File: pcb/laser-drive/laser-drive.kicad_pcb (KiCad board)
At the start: 2 copper layers, 28.6 x 32.4 mm, 29 parts, among them J1 CONN_01X03, P1 LaserOut, Q1 BCP5616Q, Q2 MTM232270, U2 MIC920

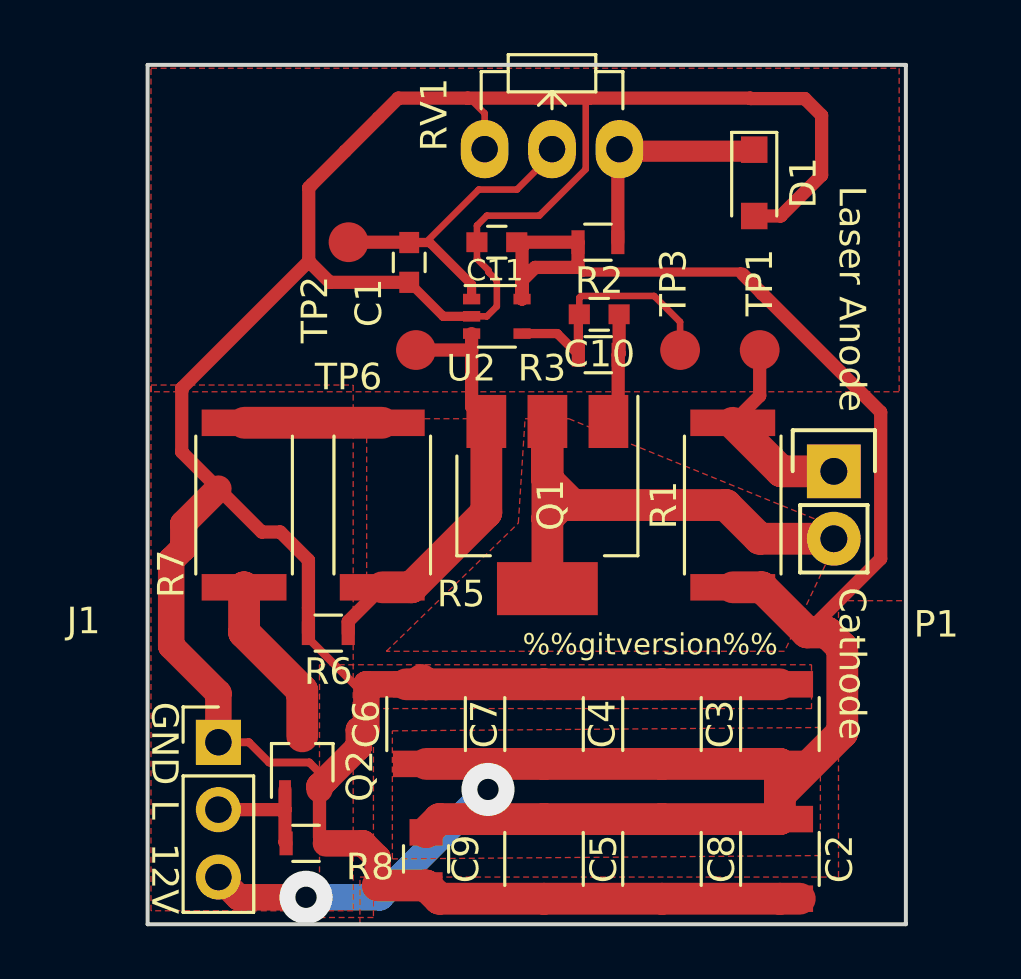
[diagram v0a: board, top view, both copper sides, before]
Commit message: Laser driver: Update to current KiCAD
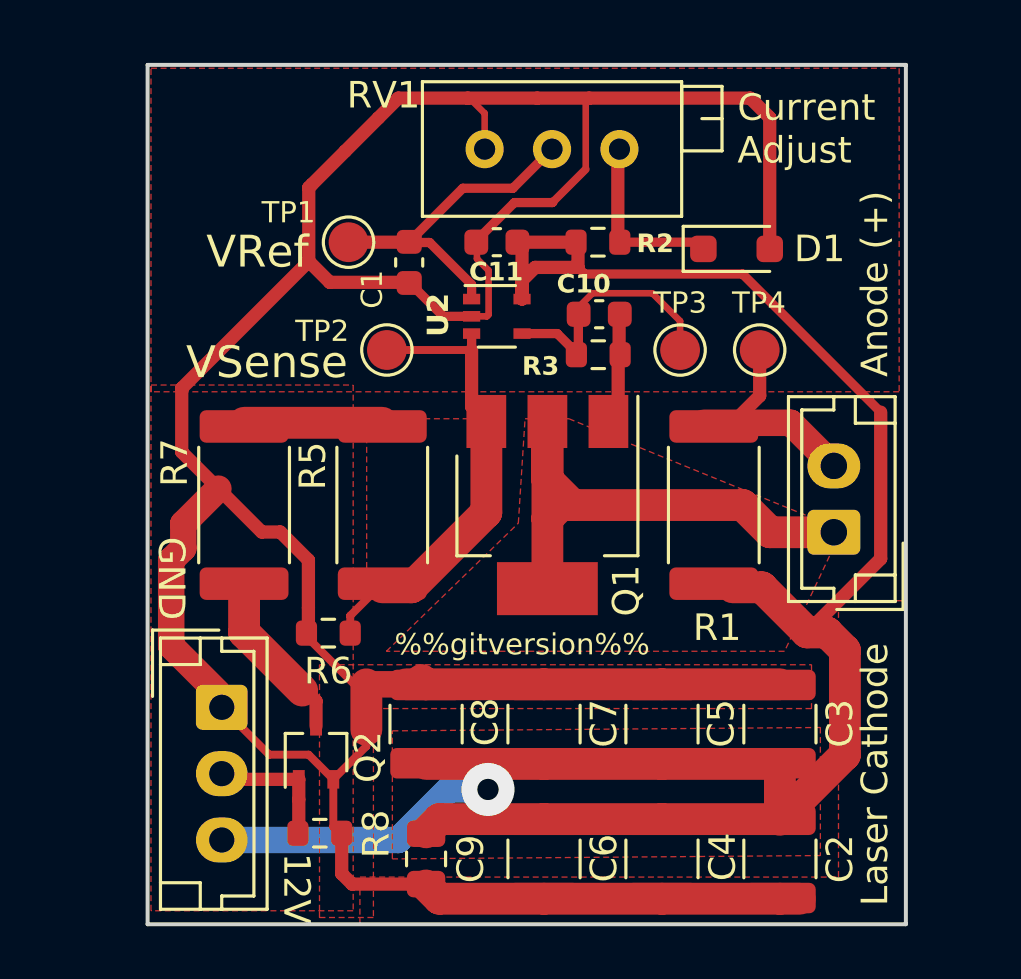
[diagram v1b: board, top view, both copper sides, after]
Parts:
- C1, C10, C11: footprint Capacitors_SMD:C_0603 -> Capacitor_SMD:C_0603_1608Metric
- C2, C3, C4, C5, C6, C7, C8: footprint Capacitors_SMD:C_1210 -> Capacitor_SMD:C_1210_3225Metric
- C9: footprint Capacitors_SMD:C_0805 -> Capacitor_SMD:C_0805_2012Metric
- D1: footprint Diodes_SMD:D_SOD-323_HandSoldering -> Diode_SMD:D_SOD-323_HandSoldering
- J1: footprint Pin_Headers:Pin_Header_Straight_1x03_Pitch2.54mm -> Connector_JST:JST_EH_B3B-EH-A_1x03_P2.50mm_Vertical
- P1: footprint Pin_Headers:Pin_Header_Straight_1x02 -> Connector_JST:JST_EH_B2B-EH-A_1x02_P2.50mm_Vertical
- Q1: footprint TO_SOT_Packages_SMD:SOT-223 -> Package_TO_SOT_SMD:SOT-223-3_TabPin2
- Q2: footprint TO_SOT_Packages_SMD:SOT-323_SC-70 -> Package_TO_SOT_SMD:SOT-323_SC-70
- R1, R5, R7: footprint Resistors_SMD:R_2512 -> Resistor_SMD:R_2512_6332Metric
- R2, R3, R6, R8: footprint Resistors_SMD:R_0603 -> Resistor_SMD:R_0603_1608Metric
- RV1: footprint Potentiometers:Potentiometer_WirePads_Small -> Potentiometer_THT:Potentiometer_Bourns_3296X_Horizontal
- TP1: renamed from TP2; footprint Measurement_Points:Measurement_Point_Round-SMD-Pad_Small -> TestPoint:TestPoint_Pad_D1.5mm
- TP2: renamed from TP6; footprint Measurement_Points:Measurement_Point_Round-SMD-Pad_Small -> TestPoint:TestPoint_Pad_D1.5mm
- TP3: footprint Measurement_Points:Measurement_Point_Round-SMD-Pad_Small -> TestPoint:TestPoint_Pad_D1.5mm
- TP4: renamed from TP1; footprint Measurement_Points:Measurement_Point_Round-SMD-Pad_Small -> TestPoint:TestPoint_Pad_D1.5mm
- U2: footprint TO_SOT_Packages_SMD:SOT-353_SC-70-5 -> Package_TO_SOT_SMD:SOT-353_SC-70-5
- moved C8 10.2 mm to (93.7, 69.9), turned to 90 degrees
- moved C5 6.75 mm to (102.6, 69.9), turned to 90 degrees
- moved C6 6.75 mm to (98.1, 75.0), turned to -90 degrees
- moved C4 5.08 mm to (102.6, 75.0), turned to -90 degrees
- moved D1 2.58 mm to (105.4, 52.0), turned to 0 degrees
- moved P1 2.30 mm to (109.0, 62.7), turned to 90 degrees
- moved J1 1.32 mm to (86.0, 69.3), turned to -90 degrees
- moved TP2 1.10 mm to (92.2, 55.8)
- moved R1 0.71 mm to (104.5, 61.7)
- moved R8 0.64 mm to (89.7, 74.0)
- moved Q2 0.64 mm to (89.5, 71.0)
- turned RV1 to 180 degrees
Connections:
- net Net-(C10-Pad2) renamed /ControlOut
- net Net-(D1-Pad1) renamed /Hot
- P1 pad 1: /CurrentTP -> /Laser-Cathode
- P1 pad 2: /LaserOut -> /Laser-Anode
- Q1 pad 2: /LaserOut -> /Laser-Cathode
- R1 pad 2: /CurrentTP -> /Laser-Anode
- TP4 pad 1: /CurrentTP -> /Laser-Anode
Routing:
- net /LaserOut: track 21.4 -> 0.00 mm
- net /Laser-Cathode: track 0.00 -> 21.3 mm
- net /Laser-Anode: track 0.00 -> 8.74 mm
- net /CurrentTP: track 7.73 -> 0.00 mm
- net GND: track 130.9 -> 125.9 mm
- net /Hot: track 9.19 -> 7.00 mm
- net /VRef: track 12.8 -> 13.5 mm
- net /VSense: track 17.0 -> 17.6 mm
- net +12V: track 85.8 -> 85.3 mm, vias 2 -> 1
- added copper zone on F.Cu, net /Laser-Cathode
- removed copper zone on F.Cu, net /LaserOut
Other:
- net class Default removed
- net class Power removed
- rule pad_to_mask_clearance: 0.2 -> 0.1
- board text added: "Anode (+)"
- board text added: "Current Adjust"
- board text added: "Laser Cathode"
- board text added: "VRef"
- board text added: "VSense"
- board text removed: "Cathode"
- board text removed: "L"
- board text removed: "Laser Anode"

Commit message: Update fab script to work with current KiCAD
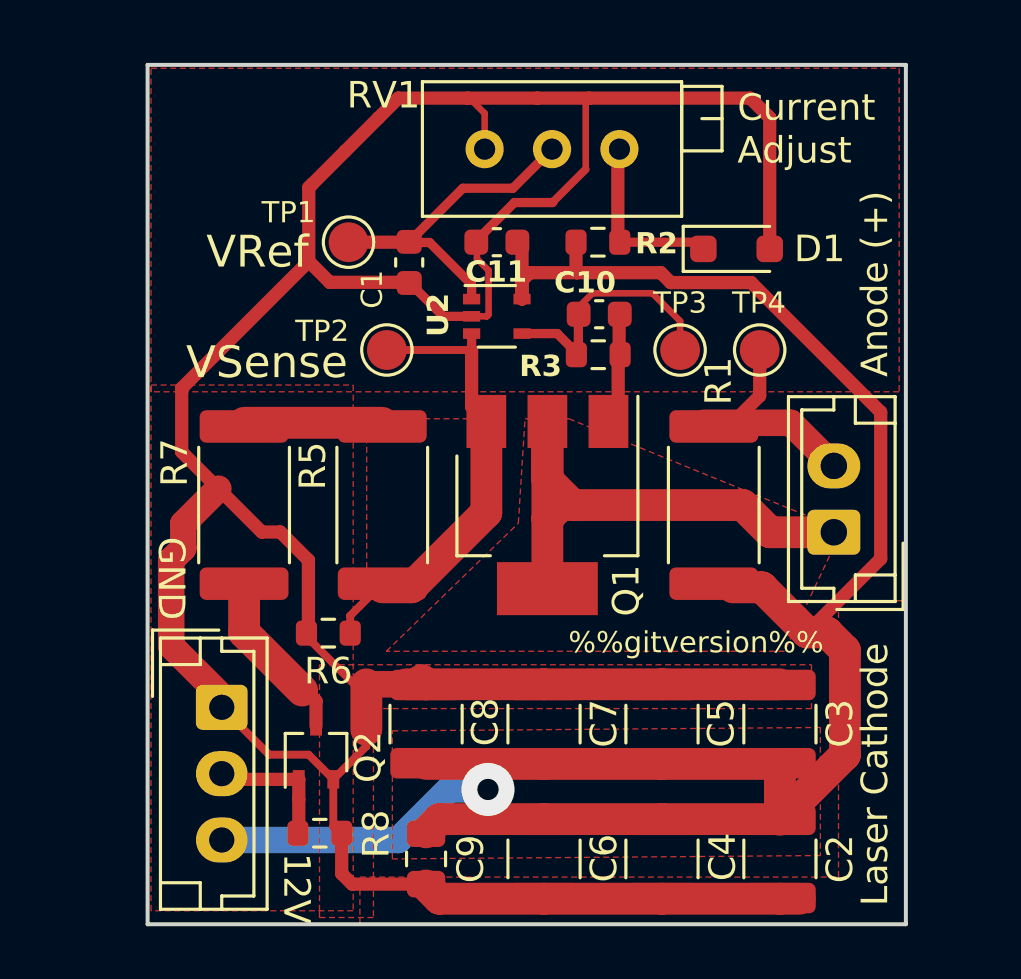
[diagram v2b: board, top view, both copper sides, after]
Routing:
- net +12V: track 85.3 -> 83.1 mm
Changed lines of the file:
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@@
     (attr smd)
     (fp_text reference "C11" (at -0.028287 1.115849 180) (layer "F.SilkS")
-        (effects (font (size 0.7 0.7) (thickness 0.12) bold))
+        (effects (font (size 0.8 0.8) (thickness 0.12) bold))
     )
     (fp_text value "100n" (at 0 1.43) (layer "F.Fab")
@@
     (property "Sheetname" "")
     (attr smd)
-    (fp_text reference "R1" (at -4.621049 0.127 180) (layer "F.SilkS")
+    (fp_text reference "R1" (at 4.675351 0.1778 90) (layer "F.SilkS")
         (effects (font (size 1 1) (thickness 0.15)))
     )
@@
     (attr smd)
     (fp_text reference "R3" (at 2.173887 -0.4318 180) (layer "F.SilkS")
-        (effects (font (size 0.7 0.7) (thickness 0.12) bold))
+        (effects (font (size 0.8 0.8) (thickness 0.12) bold))
     )
     (fp_text value "470" (at 0 1.43 180) (layer "F.Fab")
@@
     (property "Sheetname" "")
     (attr smd)
-    (fp_text reference "R2" (at 2.156113 0.049049) (layer "F.SilkS")
-        (effects (font (size 0.7 0.7) (thickness 0.12) bold))
+    (fp_text reference "R2" (at 2.206913 0.049049) (layer "F.SilkS")
+        (effects (font (size 0.8 0.8) (thickness 0.12) bold))
     )
     (fp_text value "2k2" (at 0 1.43) (layer "F.Fab")
@@
     (property "Sheetname" "")
     (attr smd)
-    (fp_text reference "C10" (at 0.5842 1.143 180) (layer "F.SilkS")
-        (effects (font (size 0.7 0.7) (thickness 0.12) bold))
+    (fp_text reference "C10" (at 0.5334 1.1938 180) (layer "F.SilkS")
+        (effects (font (size 0.8 0.8) (thickness 0.12) bold))
     )
     (fp_text value "100p" (at 0 1.43 180) (layer "F.Fab")
@@
     (effects (font (size 1 1) (thickness 0.2)) (justify left))
   )
-  (gr_text "%%gitversion%%" (at 102.108 66.929) (layer "F.SilkS")
+  (gr_text "%%gitversion%%" (at 108.6612 66.8528) (layer "F.SilkS")
     (effects (font (size 0.8 0.8) (thickness 0.15)) (justify right))
   )
@@
   (segment (start 93.515087 68.264951) (end 93.678087 68.427951) (width 1.2) (layer "F.Cu") (net 1))
   (segment (start 96.035088 52.831952) (end 96.035088 54.49595) (width 0.25) (layer "F.Cu") (net 1))
+  (segment (start 102.899216 53.2892) (end 102.526968 52.916952) (width 0.5) (layer "F.Cu") (net 2))
+  (segment (start 97.295087 53.210951) (end 97.295087 53.910951) (width 0.5) (layer "F.Cu") (net 2))
   (segment (start 109.463087 71.082951) (end 107.013087 73.532951) (width 1.2) (layer "F.Cu") (net 2))
-  (segment (start 97.295087 53.210951) (end 97.789087 52.716951) (width 0.5) (layer "F.Cu") (net 2))
-  (segment (start 108.035087 66.472951) (end 110.811088 63.69695) (width 0.5) (layer "F.Cu") (net 2))
-  (segment (start 99.405087 51.766951) (end 97.095087 51.766951) (width 0.5) (layer "F.Cu") (net 2))
   (segment (start 107.013087 72.594951) (end 107.013087 71.427951) (width 1.2) (layer "F.Cu") (net 2))
+  (segment (start 110.811088 58.17095) (end 105.929338 53.2892) (width 0.5) (layer "F.Cu") (net 2))
+  (segment (start 97.589086 52.916952) (end 97.295087 53.210951) (width 0.5) (layer "F.Cu") (net 2))
   (segment (start 96.012 73.45066) (end 95.954709 73.507951) (width 1) (layer "F.Cu") (net 2))
   (segment (start 108.035087 66.472951) (end 106.335087 64.772951) (width 1.2) (layer "F.Cu") (net 2))
   (segment (start 98.123087 71.427951) (end 93.678087 71.427951) (width 1.2) (layer "F.Cu") (net 2))
+  (segment (start 99.330087 51.766951) (end 99.330087 52.882239) (width 0.5) (layer "F.Cu") (net 2))
   (segment (start 94.178087 73.507951) (end 93.678087 74.007951) (width 1.2) (layer "F.Cu") (net 2))
   (segment (start 102.568087 73.507951) (end 98.123087 73.507951) (width 1.2) (layer "F.Cu") (net 2))
   (segment (start 109.463087 67.147949) (end 109.463087 71.082951) (width 1.2) (layer "F.Cu") (net 2))
+  (segment (start 99.3648 52.916952) (end 97.589086 52.916952) (width 0.5) (layer "F.Cu") (net 2))
   (segment (start 98.123087 73.507951) (end 95.758 73.507951) (width 1.2) (layer "F.Cu") (net 2))
   (segment (start 97.295087 53.910951) (end 97.295087 51.966951) (width 0.5) (layer "F.Cu") (net 2))
-  (segment (start 99.655088 52.966952) (end 99.405087 52.716951) (width 0.35) (layer "F.Cu") (net 2))
-  (segment (start 105.60709 52.966952) (end 99.655088 52.966952) (width 0.35) (layer "F.Cu") (net 2))
+  (segment (start 102.526968 52.916952) (end 99.3648 52.916952) (width 0.5) (layer "F.Cu") (net 2))
+  (segment (start 108.035087 66.472951) (end 110.811088 63.69695) (width 0.5) (layer "F.Cu") (net 2))
+  (segment (start 110.811088 63.69695) (end 110.811088 58.17095) (width 0.5) (layer "F.Cu") (net 2))
   (segment (start 97.295087 51.966951) (end 97.095087 51.766951) (width 0.5) (layer "F.Cu") (net 2))
-  (segment (start 110.811088 63.69695) (end 110.811088 58.17095) (width 0.5) (layer "F.Cu") (net 2))
   (segment (start 106.335087 64.772951) (end 105.235087 64.772951) (width 1.2) (layer "F.Cu") (net 2))
   (segment (start 108.788089 66.472951) (end 109.463087 67.147949) (width 1.2) (layer "F.Cu") (net 2))
   (segment (start 108.788089 66.472951) (end 108.035087 66.472951) (width 1.2) (layer "F.Cu") (net 2))
   (segment (start 107.013087 73.507951) (end 102.568087 73.507951) (width 1.2) (layer "F.Cu") (net 2))
+  (segment (start 99.330087 52.882239) (end 99.3648 52.916952) (width 0.5) (layer "F.Cu") (net 2))
   (segment (start 102.568087 71.427951) (end 98.123087 71.427951) (width 1.2) (layer "F.Cu") (net 2))
   (segment (start 107.013087 73.507951) (end 107.013087 72.594951) (width 1.2) (layer "F.Cu") (net 2))
+  (segment (start 105.929338 53.2892) (end 102.899216 53.2892) (width 0.5) (layer "F.Cu") (net 2))
   (segment (start 95.758 73.507951) (end 94.178087 73.507951) (width 1.2) (layer "F.Cu") (net 2))
-  (segment (start 97.295087 53.910951) (end 97.295087 53.210951) (width 0.5) (layer "F.Cu") (net 2))
   (segment (start 107.013087 71.427951) (end 102.568087 71.427951) (width 1.2) (layer "F.Cu") (net 2))
   (segment (start 96.012 72.39) (end 96.012 73.45066) (width 1) (layer "F.Cu") (net 2))
-  (segment (start 99.405087 51.766951) (end 99.405087 52.716951) (width 0.5) (layer "F.Cu") (net 2))
   (segment (start 95.954709 73.507951) (end 95.758 73.507951) (width 1) (layer "F.Cu") (net 2))
-  (segment (start 97.789087 52.716951) (end 99.405087 52.716951) (width 0.5) (layer "F.Cu") (net 2))
-  (segment (start 105.60709 52.966952) (end 110.811088 58.17095) (width 0.35) (layer "F.Cu") (net 2))
   (via (at 96.012 72.39) (size 2) (drill 0.8) (layers "F.Cu" "B.Cu") (net 2))
   (segment (start 94.5388 72.39) (end 96.012 72.39) (width 1) (layer "B.Cu") (net 2))
@@
   (segment (start 95.395087 53.910951) (end 95.395087 53.360951) (width 0.35) (layer "F.Cu") (net 6))
   (segment (start 93.031087 51.766951) (end 93.043087 51.778951) (width 0.5) (layer "F.Cu") (net 6))
-  (segment (start 98.425 48.26) (end 98.425 48.46) (width 0.25) (layer "F.Cu") (net 6))
   (segment (start 95.395087 53.360951) (end 93.813087 51.778951) (width 0.35) (layer "F.Cu") (net 6))
   (segment (start 95.063038 49.734) (end 93.043087 51.753951) (width 0.35) (layer "F.Cu") (net 6))
